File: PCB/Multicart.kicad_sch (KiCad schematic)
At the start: 40 parts, among them J1 DB25_Plug, SW1 RST, SW2 NEXT, U1 DS1812, U2 74HC00, U3 LM810, U4 AT89C2051-12P, U5 SST39SF040, U6 SST39SF040, U7 SST39SF040, U8 SA39-12SRWA, U9 74LS573, Y1 12MHz

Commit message: PCB updated, B will be the last revision to use 89C2051
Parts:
- removed C1: 100n, Capacitor_SMD:C_1206_3216Metric_Pad1.33x1.80mm_HandSolder, symbol Device:C
- removed R1: 10k, Resistor_SMD:R_1206_3216Metric_Pad1.30x1.75mm_HandSolder, symbol Device:R
- removed U1: DS1812, Package_TO_SOT_THT:TO-92, symbol Power_Supervisor:MCP101-270D
- removed U8: SA39-12SRWA, Display_7Segment:Sx39-1xxxxx, symbol Display_Character:SA39-12SRWA
- added C12: 100n, Capacitor_SMD:C_1206_3216Metric_Pad1.33x1.80mm_HandSolder, symbol Device:C
- added H1, H2, H3, H4, H5: ~, MountingHole:MountingHole_3.2mm_M3_DIN965, symbol Mechanical:MountingHole
- added R11, R12: 330, Resistor_SMD:R_1206_3216Metric_Pad1.30x1.75mm_HandSolder, symbol Device:R
- added R6: 10k, Resistor_SMD:R_1206_3216Metric_Pad1.30x1.75mm_HandSolder, symbol Device:R
- added U6: SA39-11SRWA, Display_7Segment:Sx39-1xxxxx, symbol Display_Character:SA39-11SRWA
- J1: value DB25_Plug -> MODULE
- SW1: value RST -> BACK
- U7: renamed from U3; value LM810 -> MAX810
- Y1: value 12MHz -> 3.6864MHz
- renumbered C6 to C1, C8 to C10, C9 to C11, C4 to C13, C5 to C4, C10 to C5, C11 to C6, C12 to C7, C13 to C8, C7 to C9, R3 to R1, R12 to R10, R14 to R13, R9 to R14, R11 to R15, R13 to R16, R4 to R2, R5 to R3, R6 to R4, R7 to R5, R2 to R7, R10 to R9, U2 to U1, U9 to U2, U5 to U3, U6 to U4, U7 to U5, U4 to U8
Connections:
- net +5V: now also R6.2, U6.3 (CA), U6.8 (CA)
- net GND: now also C12.2
- net NEXT_SW: now also R12.1; no longer SW2.2
- net at R5.2: now also U6.4 (E)
- net at R4.2: now also U6.5 (D)
- net at R9.2: now also U6.1 (G)
- net at R1.2: now also U6.10 (A)
- net at R3.2: now also U6.7 (C)
- net at R10.2: now also U6.6 (DP)
- net at R2.2: now also U6.9 (B)
- net at R8.2: now also U6.2 (F)
- net RST_SW: no longer names the net of SW1.2
- net RST_SW: now also R11.2; no longer U8.11 (P3.7)
- new net: R12.2, SW2.2
- new net BACK_SW: C12.1, R11.1, R6.1, U8.11 (P3.7)
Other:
- note removed: "check if outputs are push-pull"
- title: FLT/CU-1 multicart -> FLT/ART/CU-1 multicart
- moved on the sheet: C13, R7, SW2, U7

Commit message: Update for production
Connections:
- net GND: now also J1.0
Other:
- moved on the sheet: C2, C3, C4

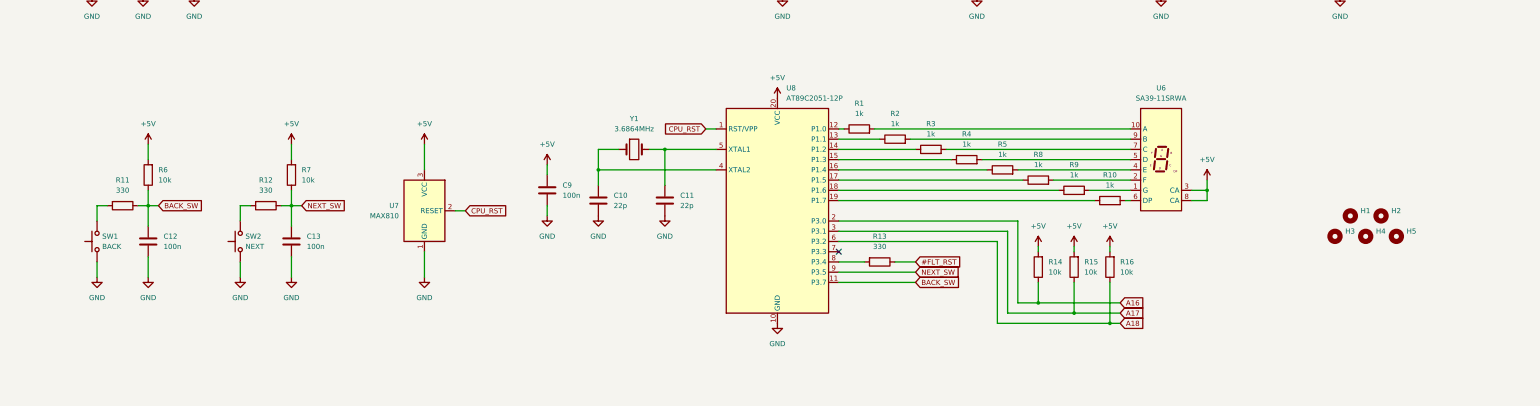
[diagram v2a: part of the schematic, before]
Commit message: MCU changed to Attiny 406/806, PCB updated to revision C
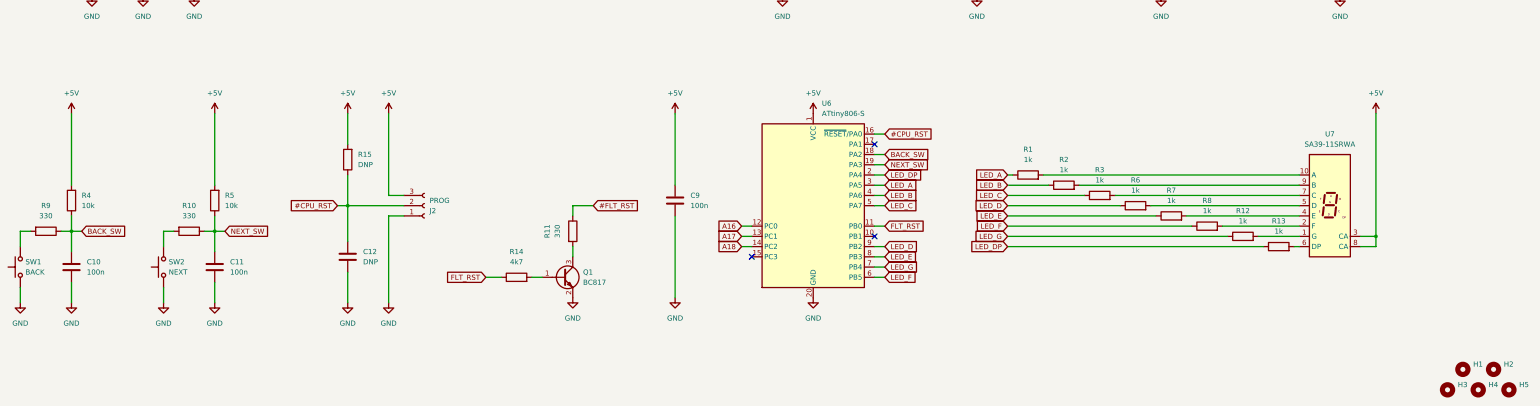
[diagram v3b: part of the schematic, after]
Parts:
- removed C10, C11: 22p, Capacitor_SMD:C_1206_3216Metric_Pad1.33x1.80mm_HandSolder, symbol Device:C
- removed R16: 10k, Resistor_SMD:R_1206_3216Metric_Pad1.30x1.75mm_HandSolder, symbol Device:R
- removed U7: MAX810, Package_TO_SOT_SMD:SOT-23, symbol Power_Supervisor:LM810
- removed U8: AT89C2051-12P, Package_DIP:DIP-20_W7.62mm, symbol MCU_Microchip_8051:AT89C2051-12P
- removed Y1: 3.6864MHz, Crystal:Crystal_HC49-4H_Vertical, symbol Device:Crystal
- added C12: DNP, Capacitor_SMD:C_1206_3216Metric_Pad1.33x1.80mm_HandSolder, symbol Device:C
- added J2: PROG, Connector_PinHeader_2.54mm:PinHeader_1x03_P2.54mm_Horizontal, symbol Connector:Conn_01x03_Socket
- added Q1: BC817, Package_TO_SOT_SMD:SOT-23_Handsoldering, symbol Transistor_BJT:BC817
- added U6: ATtiny806-S, Package_SO:SOIC-20W_7.5x12.8mm_P1.27mm, symbol MCU_Microchip_ATtiny:ATtiny806-S
- J1: footprint Connector_Dsub:DSUB-25_Male_Horizontal_P2.77x2.84mm_EdgePinOffset4.94mm_Housed_MountingHolesOffset7.48mm -> Connector_Dsub:DSUB-25_Pins_Horizontal_P2.77x2.84mm_EdgePinOffset7.70mm_Housed_MountingHolesOffset9.12mm
- R14: value 10k -> 4k7
- R15: value 10k -> DNP
- renumbered C12 to C10, C13 to C11, R12 to R10, R13 to R11, R9 to R12, R10 to R13, R6 to R4, R7 to R5, R4 to R6, R5 to R7, R11 to R9, U6 to U7
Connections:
- net +5V: now also J2.3 (Pin_3), U6.1 (VCC); no longer R14.2
- net A16: now also U6.12 (PC0); no longer R14.1
- net A17: now also U6.13 (PC1); no longer R15.1
- net A18: now also U6.14 (PC2)
- net BACK_SW: now also U6.18 (PA2)
- net GND: now also C12.2, J2.1 (Pin_1), Q1.2 (E), U6.20 (GND)
- net NEXT_SW: now also U6.19 (PA3)
- net LED_E: now reaches R7.1
- net LED_E: now also U6.8 (PB3)
- net LED_D: now reaches R6.1
- net LED_D: now also U6.9 (PB2)
- net LED_G: now reaches R12.1
- net LED_G: now also U6.7 (PB4)
- net LED_A: now reaches R1.1
- net LED_A: now also U6.3 (PA5)
- net LED_C: now reaches R3.1
- net LED_C: now also U6.5 (PA7)
- net LED_B: now reaches R2.1
- net LED_B: now also U6.4 (PA6)
- net LED_F: now reaches R8.1
- net LED_F: now also U6.6 (PB5)
- net LED_DP: now reaches R13.1
- net LED_DP: now also U6.2 (PA4)
- net at R11.2: now also Q1.3 (C)
- new net: Q1.1 (B), R14.2
- new net #CPU_RST: C12.1, J2.2 (Pin_2), R15.1, U6.16 (~{RESET}/PA0)
- new net FLT_RST: R14.1, U6.11 (PB0)
- no-connect marks 2 -> 4
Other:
- moved on the sheet: C10, C11, C9, H1, H2, H3, H4, H5, R1, R10, R11, R12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
